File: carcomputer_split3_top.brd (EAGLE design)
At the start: 107.6 x 80 mm, 39 parts, among them K1 351, Q1 BUZ10, Q2 BUZ10, T1 2N2219

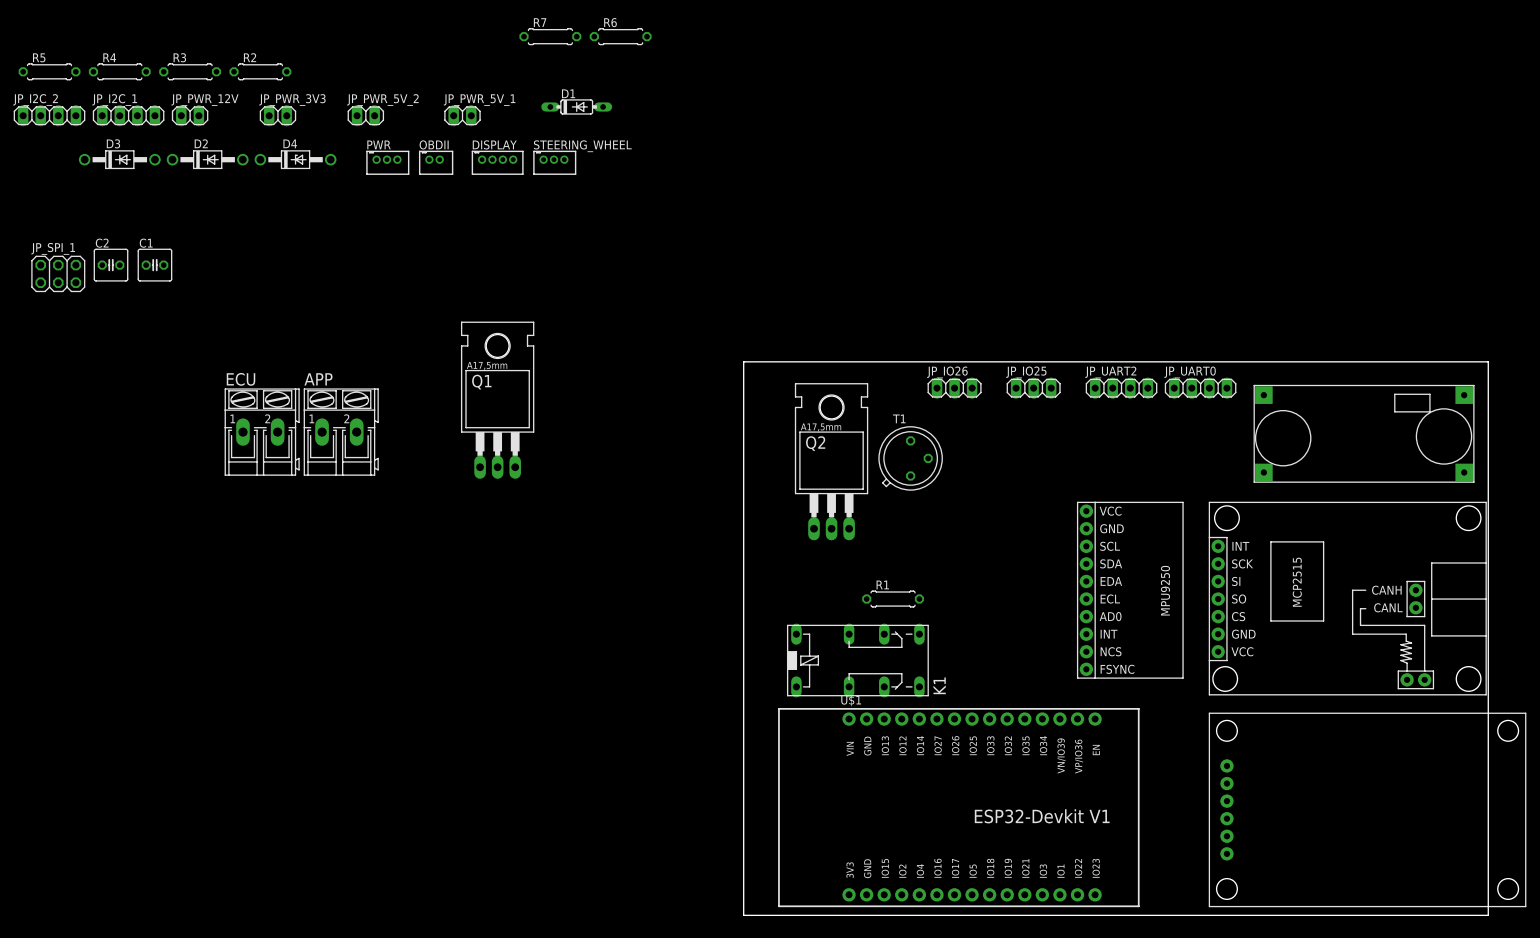
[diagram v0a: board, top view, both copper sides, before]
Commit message: some various board layout options
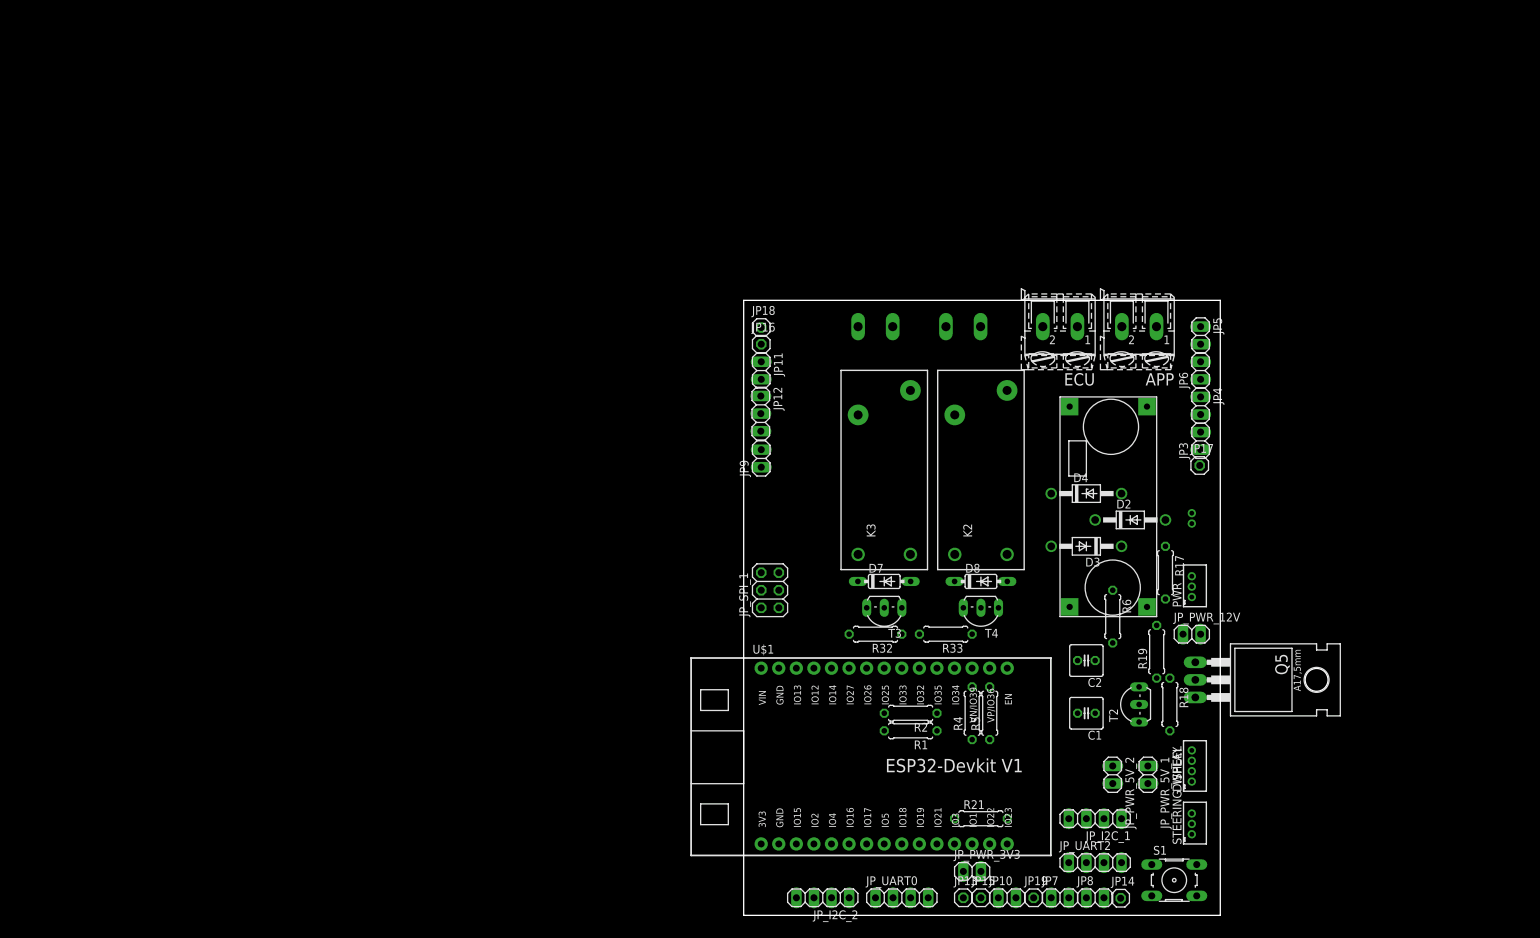
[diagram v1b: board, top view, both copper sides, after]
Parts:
- removed D1: 1N4148DO35-7, diode:DO35-7
- removed JP_IO25, JP_IO26: (no value), pinhead:1X03
- removed K1: 351, relay:351
- removed Q1, Q2: BUZ10, transistor-fet:TO220
- removed R3: 2k, rcl:0207/7
- removed R7: 10k, rcl:0207/7
- removed T1: 2N2219, transistor:TO5
- removed U$2: MCP2515_DEVBOARD, MCP2515:MCP2515_DEVBOARD
- removed U$3: MPU9250_BREAKOUT, MPU9250:MPU9250_BREAKOUT
- removed U$5: HKD-MICRO-SD-BREAKOUT, sd-mmc:HKD-MICRO-SD-BREAKOUT
- added CLAXON_CONN, ENGINE_CUTOFF_CONN: (no value), con-ptr500-custom:AK300/2
- added D7, D8: 1N4148DO35-7, diode:DO35-7
- added JP10, JP11, JP3, JP4, JP5, JP6, JP7, JP8, JP9: (no value), pinhead:1X02
- added JP12: (no value), pinhead:1X03
- added JP13, JP14, JP15, JP16, JP17, JP18, JP19: (no value), pinhead:1X01
- added K2, K3: RT184012, relay:RT-N/O12A3.5
- added Q5: TIP136, transistor-pnp:TO220
- added R17: 26k, rcl:0207/7
- added R18, R19: 10k, rcl:0207/7
- added R21: 1k, rcl:0207/7
- added R32, R33: 2k, rcl:0207/7
- added S1: (no value), switch-omron:B3F-10XX
- added T2, T3, T4: BC618, transistor-npn:TO92-EBC
- APP, ECU: device con-ptr500:AK300/2 -> con-ptr500-custom:AK300/2
- moved JP_I2C_1 172.7 mm to (50.8, 14.0), turned to 180 degrees
- moved R5 164.5 mm to (35.6, 29.2), turned to 90 degrees
- moved JP_PWR_12V 163.0 mm to (64.8, 40.6)
- moved JP_I2C_2 159.0 mm to (11.4, 2.54), turned to 180 degrees
- moved R4 154.2 mm to (33.0, 29.2), turned to 90 degrees
- moved C2 152.1 mm to (49.5, 36.8), turned to 180 degrees
- moved D3 150.5 mm to (49.5, 53.3), turned to 180 degrees
- moved C1 149.4 mm to (49.5, 29.2), turned to 180 degrees
- moved JP_PWR_3V3 148.3 mm to (33.0, 6.35)
- moved JP_PWR_5V_2 144.0 mm to (53.3, 20.3), turned to 270 degrees
- moved D2 143.2 mm to (55.9, 57.1)
- moved JP_PWR_5V_1 137.4 mm to (58.4, 20.3), turned to 270 degrees
- moved DISPLAY 133.2 mm to (64.8, 21.6), turned to 90 degrees
- moved STEERING_WHEEL 132.0 mm to (64.8, 14.0), turned to 90 degrees
- moved R2 132.0 mm to (24.1, 29.2), turned to 180 degrees
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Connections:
- net SENS_APP_0_OUT renamed APP_PWM_OUT_0
- net SENS_APP_1_OUT renamed APP_PWM_OUT_1
- removed net IO25: JP_IO25.2, U$1.D25
- removed net IO26: JP_IO26.2, U$1.D26
- removed net N$1: D1.A, K1.1, T1.3
- removed net N$2: R3.1, T1.2
- removed net N$3: C1.1, K1.S1, R2.1
- removed net N$4: C2.1, K1.S2, R1.1
- removed net N$6: ECU.2, K1.P1
- removed net N$7: ECU.1, K1.P2
- removed net PWR_IN-: Q1.2, Q2.2, U$4.IN-
- new net APP_0_IN: APP.1, JP4.2
- new net APP_1_IN: APP.2, JP4.1
- new net APP_ANALOG_OUT_0: C2.1, JP6.2, R1.1
- new net APP_ANALOG_OUT_1: C1.1, JP6.1, R2.1
- new net CLAXON_ENABLE: R33.2, U$1.D25
- new net ECU_OUT_0: ECU.1, JP5.2
- new net ECU_OUT_1: ECU.2, JP5.1
- new net ENGINE_CUTOFF_DISABLE: R32.2, U$1.D26
- new net GPS_RX: JP8.1, JP_UART2.2
- new net GPS_TX: JP8.2, JP_UART2.3
- new net MCU_RESET: JP14.1, S1.3, S1.4, U$1.EN
- new net N$11: D3.A, D4.C, R21.1
- new net N$12: D2.A, R17.1
- new net N$14: Q5.1, R18.1, R19.1
- new net N$15: R18.2, T2.C
- new net N$19: ENGINE_CUTOFF_CONN.1, K3.11
- new net N$20: ENGINE_CUTOFF_CONN.2, K3.14
- new net N$22: D7.A, K3.A1, T3.C
- new net N$23: D8.A, K2.A1, T4.C
- new net N$25: R33.1, T4.B
- new net N$26: R32.1, T3.B
- new net N$27: CLAXON_CONN.1, K2.11
- new net N$28: CLAXON_CONN.2, K2.14
- new net PWR_IN+: JP17.1, Q5.2, U$4.IN+
- net +12V: now also D7.C, D8.C, K2.A2, K3.A2, Q5.3, R19.2; no longer U$4.IN+
- net +3V3: now also DISPLAY.4, JP15.1
- net +5V: now also JP16.1; no longer D1.C, DISPLAY.4, JP_IO25.3, JP_IO26.3, K1.16, U$2.VCC, U$3.VCC, U$5.VCC
- net APP_ENABLE: now also JP13.1; no longer R3.2
- net CAN_CS: now also JP11.2; no longer U$2.CS
- net CAN_H: now also JP9.1; no longer U$2.CAN_H
- net CAN_INT: now also JP11.1; no longer U$2.INT
- net CAN_L: now also JP9.2; no longer U$2.CAN_L
- net GND: now also JP18.1, S1.1, S1.2, T2.E, T3.E, T4.E, U$4.IN-; no longer JP_IO25.1, JP_IO26.1, Q1.3, Q2.3, R7.1, T1.1, U$2.GND, U$3.FSYNC, U$3.GND, U$5.GND
- net I2C0_SCL: now also JP10.1; no longer U$3.SCL
- net I2C0_SDA: now also JP10.2; no longer U$3.SDA
- net IGNITION: now also R17.2; no longer D2.A
- net N$5: now also T2.B; no longer Q1.1
- net PWR_ENABLE: now also R21.2; no longer D3.A, D4.C, Q2.1, R7.2
- net SD_CS: now also JP19.1; no longer U$5.CS
- net SENS_APP_0_IN: now also JP3.1; no longer APP.1, K1.O2
- net SENS_APP_1_IN: now also JP3.2; no longer APP.2, K1.O1
- net SPI_MISO: now also JP12.1, U$1.D13; no longer U$1.D12, U$2.SO, U$5.MISO
- net SPI_MOSI: now also JP12.2, U$1.D12; no longer U$1.D13, U$2.SI, U$5.MOSI
- net SPI_SCK: now also JP12.3; no longer U$2.SCK, U$5.SCK
- net UART2_RX: now also JP7.2; no longer JP_UART2.2
- net UART2_TX: now also JP7.1; no longer JP_UART2.3
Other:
- board size 107.6 x 80 mm -> 68.9 x 88.9 mm
